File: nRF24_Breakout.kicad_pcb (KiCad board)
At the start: 2 copper layers, 2 parts, among them J1 Conn_01x08_Male, U1 nRF24

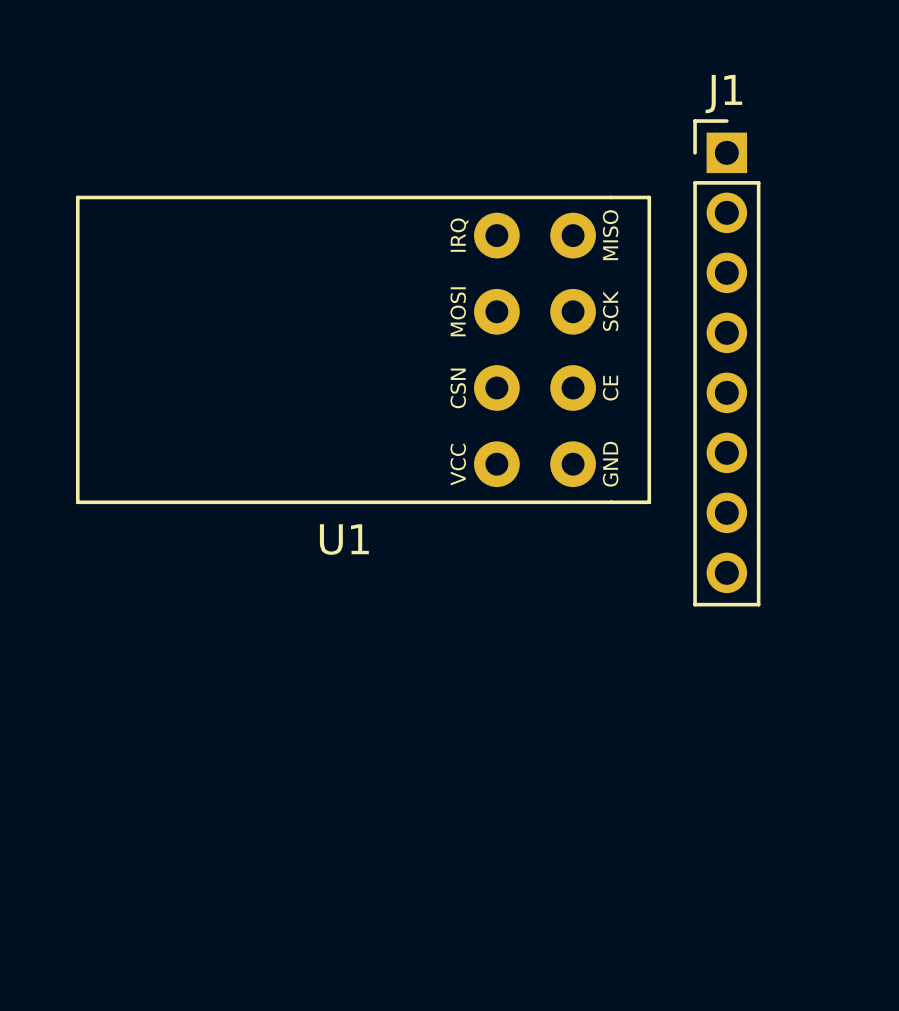
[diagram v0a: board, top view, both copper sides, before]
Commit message: Updated Connector Pins
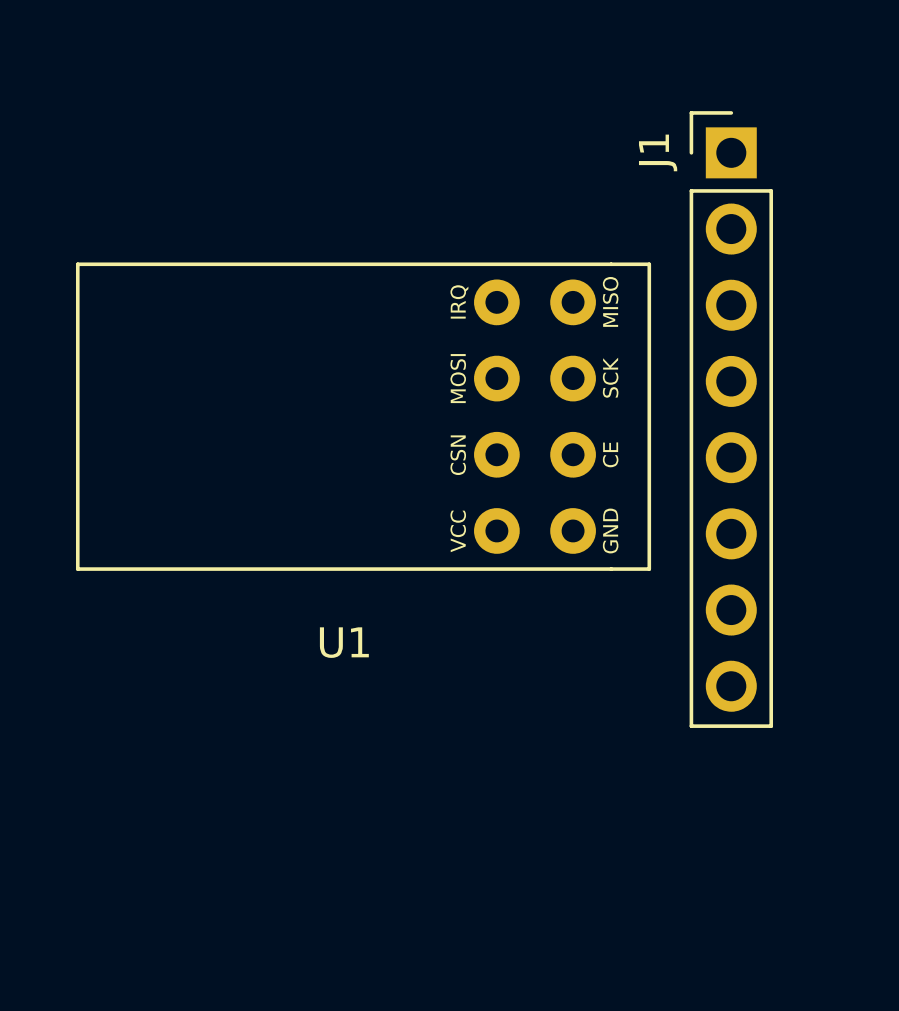
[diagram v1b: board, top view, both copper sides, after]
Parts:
- J1: value Conn_01x08_Male -> Conn_01x08_Female; footprint Connector_PinHeader_2.00mm:PinHeader_1x08_P2.00mm_Vertical -> Connector_PinHeader_2.54mm:PinHeader_1x08_P2.54mm_Vertical
- moved U1 2.23 mm to (139.0, 99.6)
- moved J1 0.15 mm to (151.9, 89.5)
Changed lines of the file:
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@@
   (general
     (thickness 1.6)
-    (drawings 0)
+    (drawings 7)
     (tracks 0)
     (zones 0)
@@
     (pad_to_mask_clearance 0)
     (aux_axis_origin 0 0)
-    (visible_elements FFFFFF7F)
+    (visible_elements 7FFFFFFF)
     (pcbplotparams
       (layerselection 0x010fc_ffffffff)
@@
     (add_net "Net-(J1-Pad8)")
   )
-  (module Connector_PinHeader_2.00mm:PinHeader_1x08_P2.00mm_Vertical (layer F.Cu)
-    (at 151.743001 89.504)
-    (descr "Through hole straight pin header, 1x08, 2.00mm pitch, single row")
-    (tags "Through hole pin header THT 1x08 2.00mm single row")
-    (fp_text reference J1 (at 0 -2.06) (layer F.SilkS)
-      (effects (font (size 1 1) (thickness 0.15)))
-    )
-    (fp_text value Conn_01x08_Male (at 0 16.06) (layer F.Fab)
-      (effects (font (size 1 1) (thickness 0.15)))
-    )
-    (fp_line (start 1.5 -1.5) (end -1.5 -1.5) (layer F.CrtYd) (width 0.05))
-    (fp_line (start 1.5 15.5) (end 1.5 -1.5) (layer F.CrtYd) (width 0.05))
-    (fp_line (start -1.5 15.5) (end 1.5 15.5) (layer F.CrtYd) (width 0.05))
-    (fp_line (start -1.5 -1.5) (end -1.5 15.5) (layer F.CrtYd) (width 0.05))
-    (fp_line (start -1.06 -1.06) (end 0 -1.06) (layer F.SilkS) (width 0.12))
-    (fp_line (start -1.06 0) (end -1.06 -1.06) (layer F.SilkS) (width 0.12))
-    (fp_line (start -1.06 1) (end 1.06 1) (layer F.SilkS) (width 0.12))
-    (fp_line (start 1.06 1) (end 1.06 15.06) (layer F.SilkS) (width 0.12))
-    (fp_line (start -1.06 1) (end -1.06 15.06) (layer F.SilkS) (width 0.12))
-    (fp_line (start -1.06 15.06) (end 1.06 15.06) (layer F.SilkS) (width 0.12))
-    (fp_line (start -1 -0.5) (end -0.5 -1) (layer F.Fab) (width 0.1))
-    (fp_line (start -1 15) (end -1 -0.5) (layer F.Fab) (width 0.1))
-    (fp_line (start 1 15) (end -1 15) (layer F.Fab) (width 0.1))
-    (fp_line (start 1 -1) (end 1 15) (layer F.Fab) (width 0.1))
-    (fp_line (start -0.5 -1) (end 1 -1) (layer F.Fab) (width 0.1))
-    (fp_text user %R (at 0 7 90) (layer F.Fab)
-      (effects (font (size 1 1) (thickness 0.15)))
-    )
-    (pad 1 thru_hole rect (at 0 0) (size 1.35 1.35) (drill 0.8) (layers *.Cu *.Mask)
+  (module Connector_PinHeader_2.54mm:PinHeader_1x08_P2.54mm_Vertical (layer F.Cu)
+    (at 151.892 89.504)
+    (descr "Through hole straight pin header, 1x08, 2.54mm pitch, single row")
+    (tags "Through hole pin header THT 1x08 2.54mm single row")
+    (fp_text reference J1 (at -2.54 -0.096 90) (layer F.SilkS)
+      (effects (font (size 1 1) (thickness 0.15)))
+    )
+    (fp_text value Conn_01x08_Female (at 4.572 8.032 90) (layer F.Fab) hide
+      (effects (font (size 1 1) (thickness 0.15)))
+    )
+    (fp_text user %R (at 0 8.89 90) (layer F.Fab)
+      (effects (font (size 1 1) (thickness 0.15)))
+    )
+    (fp_line (start -0.635 -1.27) (end 1.27 -1.27) (layer F.Fab) (width 0.1))
+    (fp_line (start 1.27 -1.27) (end 1.27 19.05) (layer F.Fab) (width 0.1))
+    (fp_line (start 1.27 19.05) (end -1.27 19.05) (layer F.Fab) (width 0.1))
+    (fp_line (start -1.27 19.05) (end -1.27 -0.635) (layer F.Fab) (width 0.1))
+    (fp_line (start -1.27 -0.635) (end -0.635 -1.27) (layer F.Fab) (width 0.1))
+    (fp_line (start -1.33 19.11) (end 1.33 19.11) (layer F.SilkS) (width 0.12))
+    (fp_line (start -1.33 1.27) (end -1.33 19.11) (layer F.SilkS) (width 0.12))
+    (fp_line (start 1.33 1.27) (end 1.33 19.11) (layer F.SilkS) (width 0.12))
+    (fp_line (start -1.33 1.27) (end 1.33 1.27) (layer F.SilkS) (width 0.12))
+    (fp_line (start -1.33 0) (end -1.33 -1.33) (layer F.SilkS) (width 0.12))
+    (fp_line (start -1.33 -1.33) (end 0 -1.33) (layer F.SilkS) (width 0.12))
+    (fp_line (start -1.8 -1.8) (end -1.8 19.55) (layer F.CrtYd) (width 0.05))
+    (fp_line (start -1.8 19.55) (end 1.8 19.55) (layer F.CrtYd) (width 0.05))
+    (fp_line (start 1.8 19.55) (end 1.8 -1.8) (layer F.CrtYd) (width 0.05))
+    (fp_line (start 1.8 -1.8) (end -1.8 -1.8) (layer F.CrtYd) (width 0.05))
+    (pad 8 thru_hole oval (at 0 17.78) (size 1.7 1.7) (drill 1) (layers *.Cu *.Mask)
+      (net 8 "Net-(J1-Pad8)"))
+    (pad 7 thru_hole oval (at 0 15.24) (size 1.7 1.7) (drill 1) (layers *.Cu *.Mask)
+      (net 7 "Net-(J1-Pad7)"))
+    (pad 6 thru_hole oval (at 0 12.7) (size 1.7 1.7) (drill 1) (layers *.Cu *.Mask)
+      (net 6 "Net-(J1-Pad6)"))
+    (pad 5 thru_hole oval (at 0 10.16) (size 1.7 1.7) (drill 1) (layers *.Cu *.Mask)
+      (net 5 "Net-(J1-Pad5)"))
+    (pad 4 thru_hole oval (at 0 7.62) (size 1.7 1.7) (drill 1) (layers *.Cu *.Mask)
+      (net 4 "Net-(J1-Pad4)"))
+    (pad 3 thru_hole oval (at 0 5.08) (size 1.7 1.7) (drill 1) (layers *.Cu *.Mask)
+      (net 3 "Net-(J1-Pad3)"))
+    (pad 2 thru_hole oval (at 0 2.54) (size 1.7 1.7) (drill 1) (layers *.Cu *.Mask)
+      (net 2 "Net-(J1-Pad2)"))
+    (pad 1 thru_hole rect (at 0 0) (size 1.7 1.7) (drill 1) (layers *.Cu *.Mask)
       (net 1 "Net-(J1-Pad1)"))
-    (pad 2 thru_hole oval (at 0 2) (size 1.35 1.35) (drill 0.8) (layers *.Cu *.Mask)
-      (net 2 "Net-(J1-Pad2)"))
-    (pad 3 thru_hole oval (at 0 4) (size 1.35 1.35) (drill 0.8) (layers *.Cu *.Mask)
-      (net 3 "Net-(J1-Pad3)"))
-    (pad 4 thru_hole oval (at 0 6) (size 1.35 1.35) (drill 0.8) (layers *.Cu *.Mask)
-      (net 4 "Net-(J1-Pad4)"))
-    (pad 5 thru_hole oval (at 0 8) (size 1.35 1.35) (drill 0.8) (layers *.Cu *.Mask)
-      (net 5 "Net-(J1-Pad5)"))
-    (pad 6 thru_hole oval (at 0 10) (size 1.35 1.35) (drill 0.8) (layers *.Cu *.Mask)
-      (net 6 "Net-(J1-Pad6)"))
-    (pad 7 thru_hole oval (at 0 12) (size 1.35 1.35) (drill 0.8) (layers *.Cu *.Mask)
-      (net 7 "Net-(J1-Pad7)"))
-    (pad 8 thru_hole oval (at 0 14) (size 1.35 1.35) (drill 0.8) (layers *.Cu *.Mask)
-      (net 8 "Net-(J1-Pad8)"))
-    (model ${KISYS3DMOD}/Connector_PinHeader_2.00mm.3dshapes/PinHeader_1x08_P2.00mm_Vertical.wrl
+    (model ${KISYS3DMOD}/Connector_PinHeader_2.54mm.3dshapes/PinHeader_1x08_P2.54mm_Vertical.wrl
       (at (xyz 0 0 0))
       (scale (xyz 1 1 1))
@@
   )
   (module nRF24_Breakout_footprint:nRF24 (layer F.Cu)
-    (at 138.998001 97.342001)
+    (at 138.998001 99.568)
     (descr "A footprint for the generic nRF24 module")
-    (fp_text reference U1 (at 0 5.08) (layer F.SilkS)
+    (fp_text reference U1 (at 0 6.289999) (layer F.SilkS)
       (effects (font (size 1 1) (thickness 0.15)))
     )
@@
       (effects (font (size 1 1) (thickness 0.15)))
     )
+    (fp_line (start 8.89 -6.35) (end -8.89 -6.35) (layer F.SilkS) (width 0.12))
+    (fp_line (start -8.89 -6.35) (end -8.89 3.81) (layer F.SilkS) (width 0.12))
+    (fp_line (start -8.89 3.81) (end 8.89 3.81) (layer F.SilkS) (width 0.12))
+    (fp_line (start 10.16 3.81) (end 10.16 -6.35) (layer F.SilkS) (width 0.12))
+    (fp_line (start 8.89 -6.35) (end 10.16 -6.35) (layer F.SilkS) (width 0.12))
     (fp_line (start 10.16 3.81) (end 8.89 3.81) (layer F.SilkS) (width 0.12))
-    (fp_line (start 8.89 -6.35) (end 10.16 -6.35) (layer F.SilkS) (width 0.12))
-    (fp_line (start 10.16 3.81) (end 10.16 -6.35) (layer F.SilkS) (width 0.12))
-    (fp_line (start -8.89 3.81) (end 8.89 3.81) (layer F.SilkS) (width 0.12))
-    (fp_line (start -8.89 -6.35) (end -8.89 3.81) (layer F.SilkS) (width 0.12))
-    (fp_line (start 8.89 -6.35) (end -8.89 -6.35) (layer F.SilkS) (width 0.12))
     (fp_text user GND (at 8.89 2.54 90) (layer F.SilkS)
       (effects (font (size 0.5 0.5) (thickness 0.125)))
@@
       (net 1 "Net-(J1-Pad1)"))
   )
+  (gr_line (start 154.432 109.22) (end 153.924 109.22) (layer Dwgs.User) (width 0.15))
+  (gr_line (start 154.432 87.376) (end 154.432 109.22) (layer Dwgs.User) (width 0.15))
+  (gr_line (start 153.924 87.376) (end 154.432 87.376) (layer Dwgs.User) (width 0.15))
+  (gr_line (start 129.54 109.22) (end 153.924 109.22) (layer Dwgs.User) (width 0.15))
+  (gr_line (start 129.54 105.664) (end 129.54 109.22) (layer Dwgs.User) (width 0.15))
+  (gr_line (start 129.54 87.376) (end 129.54 105.664) (layer Dwgs.User) (width 0.15))
+  (gr_line (start 153.924 87.376) (end 129.54 87.376) (layer Dwgs.User) (width 0.15))
 )

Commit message: Added tracks & labels
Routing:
- net Net-(J1-Pad1): track 0.00 -> 43.5 mm
- net Net-(J1-Pad5): track 0.00 -> 21.1 mm
- net Net-(J1-Pad2): track 0.00 -> 13.2 mm
- net Net-(J1-Pad3): track 0.00 -> 11.7 mm
- net Net-(J1-Pad7): track 0.00 -> 10.9 mm
- net Net-(J1-Pad6): track 0.00 -> 10.9 mm
- net Net-(J1-Pad8): track 0.00 -> 9.96 mm
- net Net-(J1-Pad4): track 0.00 -> 7.11 mm
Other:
- board text added: "CE"
- board text added: "CSN"
- board text added: "GND"
- board text added: "IRQ"
- board text added: "MISO"
- board text added: "MOSI"
- board text added: "SCK"
- board text added: "V1.0"
- board text added: "Vcc"
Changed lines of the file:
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@@
   (general
     (thickness 1.6)
-    (drawings 7)
-    (tracks 0)
+    (drawings 18)
+    (tracks 42)
     (zones 0)
     (modules 2)
@@
     (descr "Through hole straight pin header, 1x08, 2.54mm pitch, single row")
     (tags "Through hole pin header THT 1x08 2.54mm single row")
-    (fp_text reference J1 (at -2.54 -0.096 90) (layer F.SilkS)
+    (fp_text reference J1 (at 2.286 -0.096) (layer F.SilkS)
       (effects (font (size 1 1) (thickness 0.15)))
     )
-    (fp_text value Conn_01x08_Female (at 4.572 8.032 90) (layer F.Fab) hide
-      (effects (font (size 1 1) (thickness 0.15)))
+    (fp_text value Conn_01x08_Female (at 2.794 9.302 90) (layer F.Fab) hide
+      (effects (font (size 0.5 0.5) (thickness 0.125)))
     )
     (fp_text user %R (at 0 8.89 90) (layer F.Fab)
@@
       (net 1 "Net-(J1-Pad1)"))
   )
+  (gr_text V1.0 (at 131.318 107.696) (layer F.SilkS)
+    (effects (font (size 0.6 0.6) (thickness 0.15)))
+  )
+  (gr_text "GND\n" (at 149.86 89.408 90) (layer F.SilkS)
+    (effects (font (size 0.6 0.6) (thickness 0.15)))
+  )
+  (gr_text CE (at 149.86 91.948 90) (layer F.SilkS)
+    (effects (font (size 0.6 0.6) (thickness 0.15)))
+  )
+  (gr_text SCK (at 149.86 94.488 90) (layer F.SilkS)
+    (effects (font (size 0.6 0.6) (thickness 0.15)))
+  )
+  (gr_text MISO (at 149.86 97.028 90) (layer F.SilkS)
+    (effects (font (size 0.6 0.6) (thickness 0.15)))
+  )
+  (gr_text IRQ (at 149.86 99.568 90) (layer F.SilkS)
+    (effects (font (size 0.6 0.6) (thickness 0.15)))
+  )
+  (gr_text Vcc (at 149.86 107.188 90) (layer F.SilkS)
+    (effects (font (size 0.6 0.6) (thickness 0.15)))
+  )
+  (gr_text CSN (at 149.86 104.648 90) (layer F.SilkS)
+    (effects (font (size 0.6 0.6) (thickness 0.15)))
+  )
+  (gr_text MOSI (at 149.86 102.108 90) (layer F.SilkS)
+    (effects (font (size 0.6 0.6) (thickness 0.15)))
+  )
+  (gr_line (start 155.448 109.22) (end 154.432 109.22) (layer Dwgs.User) (width 0.15))
+  (gr_line (start 155.448 87.376) (end 155.448 109.22) (layer Dwgs.User) (width 0.15))
+  (gr_line (start 154.432 87.376) (end 155.448 87.376) (layer Dwgs.User) (width 0.15))
   (gr_line (start 154.432 109.22) (end 153.924 109.22) (layer Dwgs.User) (width 0.15))
-  (gr_line (start 154.432 87.376) (end 154.432 109.22) (layer Dwgs.User) (width 0.15))
   (gr_line (start 153.924 87.376) (end 154.432 87.376) (layer Dwgs.User) (width 0.15))
   (gr_line (start 129.54 109.22) (end 153.924 109.22) (layer Dwgs.User) (width 0.15))
@@
   (gr_line (start 129.54 87.376) (end 129.54 105.664) (layer Dwgs.User) (width 0.15))
   (gr_line (start 153.924 87.376) (end 129.54 87.376) (layer Dwgs.User) (width 0.15))
+  (segment (start 152.456001 103.568999) (end 153.067001 104.179999) (width 0.25) (layer F.Cu) (net 1))
+  (segment (start 148.079 103.568999) (end 152.456001 103.568999) (width 0.25) (layer F.Cu) (net 1))
+  (segment (start 153.067001 104.179999) (end 153.067001 108.298999) (width 0.25) (layer F.Cu) (net 1))
+  (segment (start 146.618001 102.108) (end 148.079 103.568999) (width 0.25) (layer F.Cu) (net 1))
+  (segment (start 152.906999 108.459001) (end 148.591001 108.459001) (width 0.25) (layer F.Cu) (net 1))
+  (segment (start 153.067001 108.298999) (end 152.906999 108.459001) (width 0.25) (layer F.Cu) (net 1))
+  (segment (start 147.453239 89.504) (end 151.892 89.504) (width 0.25) (layer F.Cu) (net 1))
+  (segment (start 142.991 93.966239) (end 147.453239 89.504) (width 0.25) (layer F.Cu) (net 1))
+  (segment (start 142.991 102.859) (end 142.991 93.966239) (width 0.25) (layer F.Cu) (net 1))
+  (segment (start 148.591001 108.459001) (end 142.991 102.859) (width 0.25) (layer F.Cu) (net 1))
+  (segment (start 147.453239 92.044) (end 151.892 92.044) (width 0.25) (layer F.Cu) (net 2))
+  (segment (start 145.531 93.966239) (end 147.453239 92.044) (width 0.25) (layer F.Cu) (net 2))
+  (segment (start 145.531 98.480999) (end 145.531 93.966239) (width 0.25) (layer F.Cu) (net 2))
+  (segment (start 146.618001 99.568) (end 145.531 98.480999) (width 0.25) (layer F.Cu) (net 2))
+  (segment (start 147.889002 98.299001) (end 153.160999 98.299001) (width 0.25) (layer F.Cu) (net 3))
+  (segment (start 146.618001 97.028) (end 147.889002 98.299001) (width 0.25) (layer F.Cu) (net 3))
+  (segment (start 153.160999 98.299001) (end 153.67 97.79) (width 0.25) (layer F.Cu) (net 3))
+  (segment (start 153.67 96.362) (end 151.892 94.584) (width 0.25) (layer F.Cu) (net 3))
+  (segment (start 153.67 97.79) (end 153.67 96.362) (width 0.25) (layer F.Cu) (net 3))
+  (segment (start 149.448 97.124) (end 151.892 97.124) (width 0.25) (layer F.Cu) (net 4))
+  (segment (start 148.844 96.52) (end 149.448 97.124) (width 0.25) (layer F.Cu) (net 4))
+  (segment (start 148.844 95.25) (end 148.844 96.52) (width 0.25) (layer F.Cu) (net 4))
+  (segment (start 148.082 94.488) (end 148.844 95.25) (width 0.25) (layer F.Cu) (net 4))
+  (segment (start 146.618001 94.488) (end 148.082 94.488) (width 0.25) (layer F.Cu) (net 4))
+  (segment (start 147.697002 90.868999) (end 152.590999 90.868999) (width 0.25) (layer F.Cu) (net 5))
+  (segment (start 144.078001 94.488) (end 147.697002 90.868999) (width 0.25) (layer F.Cu) (net 5))
+  (segment (start 153.094081 99.664) (end 151.892 99.664) (width 0.25) (layer F.Cu) (net 5))
+  (segment (start 154.120009 98.638072) (end 153.094081 99.664) (width 0.25) (layer F.Cu) (net 5))
+  (segment (start 154.12001 92.39801) (end 154.120009 98.638072) (width 0.25) (layer F.Cu) (net 5))
+  (segment (start 152.590999 90.868999) (end 154.12001 92.39801) (width 0.25) (layer F.Cu) (net 5))
+  (segment (start 150.708999 101.020999) (end 151.892 102.204) (width 0.25) (layer F.Cu) (net 6))
+  (segment (start 146.462238 101.020999) (end 150.708999 101.020999) (width 0.25) (layer F.Cu) (net 6))
+  (segment (start 145.531 100.089761) (end 146.462238 101.020999) (width 0.25) (layer F.Cu) (net 6))
+  (segment (start 145.531 99.412237) (end 145.531 100.089761) (width 0.25) (layer F.Cu) (net 6))
+  (segment (start 144.078001 97.959238) (end 145.531 99.412237) (width 0.25) (layer F.Cu) (net 6))
+  (segment (start 144.078001 97.028) (end 144.078001 97.959238) (width 0.25) (layer F.Cu) (net 6))
+  (segment (start 147.645239 104.744) (end 151.892 104.744) (width 0.25) (layer F.Cu) (net 7))
+  (segment (start 145.165002 102.263763) (end 147.645239 104.744) (width 0.25) (layer F.Cu) (net 7))
+  (segment (start 145.165002 100.655001) (end 145.165002 102.263763) (width 0.25) (layer F.Cu) (net 7))
+  (segment (start 144.078001 99.568) (end 145.165002 100.655001) (width 0.25) (layer F.Cu) (net 7))
+  (segment (start 149.254001 107.284) (end 151.892 107.284) (width 0.25) (layer F.Cu) (net 8))
+  (segment (start 144.078001 102.108) (end 149.254001 107.284) (width 0.25) (layer F.Cu) (net 8))
 )
